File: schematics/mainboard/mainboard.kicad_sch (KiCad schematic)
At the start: 105 parts, among them J1 SD_Card_Receptacle, J2 LCD_CONN, J3 USB_C_Receptacle_USB2.0_16P, J4 BATTERY_CONN, J5 527461671, J6 SPEAKER_CONN, J9 AudioJack3, P1 1-1473005-4, U1 AMS1117-3.3, U10 PCA9555PW, U2 AMS1117-3.3, U3 MAX3421EETJ_T, U5 AMS1117-1.8, U6 TPS63002, U7 BQ24072RGT, U9 TPS22917DBV, Y1 12MHz

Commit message: Some work on mainboard pcb, most bodges resolved.
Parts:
- added C44: 0.1uF, Capacitor_SMD:C_0805_2012Metric_Pad1.18x1.45mm_HandSolder, symbol Device:C
- added C45: 47uF, Capacitor_Tantalum_SMD:CP_EIA-3216-18_Kemet-A, symbol Device:C_Polarized
- added C46, C47: 47uF, Capacitor_SMD:C_0805_2012Metric_Pad1.18x1.45mm_HandSolder, symbol Device:C
- added FB1: FerriteBead, Inductor_SMD:L_Ferrocore_DLG-0504, symbol Device:FerriteBead
- added J7: Conn_01x06, Connector_PinHeader_2.54mm:PinHeader_1x06_P2.54mm_Vertical, symbol Connector_Generic:Conn_01x06
- added R29: 0, Resistor_SMD:R_0805_2012Metric_Pad1.20x1.40mm_HandSolder, symbol Device:R
- added U12: ADS1113IDGS, Package_SO:TSSOP-10_3x3mm_P0.5mm, symbol Analog_ADC:ADS1113IDGS
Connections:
- net 3V3: now also C44.1, U12.8 (VDD)
- net 5V0: now also C45.1, FB1.2; no longer U6.1 (VOUT), U6.10 (FB)
- net BAT+: now also U12.4 (AIN0)
- net GND: now also C44.2, C45.2, J7.1 (Pin_1), U12.1 (ADDR), U12.3 (GND), U12.5 (AIN1)
- net I2C_SCL: now also U12.10 (SCL)
- net I2C_SDA: now also U12.9 (SDA)
- net USB_VBUS: now also R29.2
- net at J9.R: now also C47.2; no longer U8.30 (HPR)
- net at U8.27 (HPL): now also C47.1; no longer J9.T
- net at C5.2, U3.22 (VBCOMP): now also R29.1
- net at P1.74: now also J7.2 (Pin_2)
- net at P1.76: now also J7.3 (Pin_3)
- net at P1.78: now also J7.4 (Pin_4)
- net at P1.80: now also J7.5 (Pin_5)
- net at P1.82: now also J7.6 (Pin_6)
- net LCD_PROG_DATA: no longer names the net of J2.37 (Pin_37)
- net LCD_PROG_DATA: no longer P1.104
- net LCD_TOUCH_CLK: no longer names the net of J2.23 (Pin_23)
- net LCD_TOUCH_CLK: no longer P1.102
- net LCD_TOUCH_DATA: no longer names the net of J2.19 (Pin_19)
- net LCD_TOUCH_DATA: no longer P1.100
- net LCD_TOUCH_INTERRUPT: no longer names the net of J2.13 (Pin_13)
- net LCD_TOUCH_INTERRUPT: no longer P1.98
- new net: C46.2, J9.T
- new net: C46.1, U8.30 (HPR)
- new net: FB1.1, U6.1 (VOUT), U6.10 (FB)
- no-connect marks 103 -> 107
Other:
- note added: "I2C address 0x48"
- note added: "TODO Battery ADC Charge signal to FPGA (open drain?) What if battery/USB are connected at the same time as "ice" USB? Power switch, larger? Headphone detection, MIC/VOLDET need to be pulled down from a R to MIC Headphone caps on +/- Done Improved bulk and filter of 5V"
- company: (none) -> Anders Pistol
- title: (none) -> RetroDÄCK
- moved on the sheet: C16, C29, C5

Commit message: More work on mainboard, mostly done but need double checking.
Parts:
- removed FB1: FerriteBead, Inductor_SMD:L_Ferrocore_DLG-0504, symbol Device:FerriteBead
- removed J9: AudioJack3, Connector_Audio:Jack_3.5mm_Switronic_ST-005-G_horizontal, symbol Connector_Audio:AudioJack3
- added R31: 10k, Resistor_SMD:R_0603_1608Metric_Pad0.98x0.95mm_HandSolder, symbol Device:R
- added U11: ~, ap_phonejack:PJ-327E-5A, symbol ap_phonejack:PJ_1
- R26: value 68 -> 120
- R27: value 30 -> 68
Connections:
- net 5V0: now also U6.1 (VOUT), U6.10 (FB)
- net GND: now also U11.1 (GND)
- net at C47.2: now also U11.3 (R)
- net at C46.2: now also U11.4 (S)
- net at P1.74: now also J7.6 (Pin_6); no longer J7.2 (Pin_2)
- net at P1.76: now also J7.5 (Pin_5); no longer J7.3 (Pin_3)
- net at P1.80: now also J7.3 (Pin_3); no longer J7.5 (Pin_5)
- net at P1.82: now also J7.2 (Pin_2); no longer J7.6 (Pin_6)
- net at U8.11 (VOL/MICDET): now also R31.2, U11.5 (DETECT_GND)
- net at U8.12 (MICBIAS): now also R31.1
- no-connect marks 107 -> 106
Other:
- moved on the sheet: J7

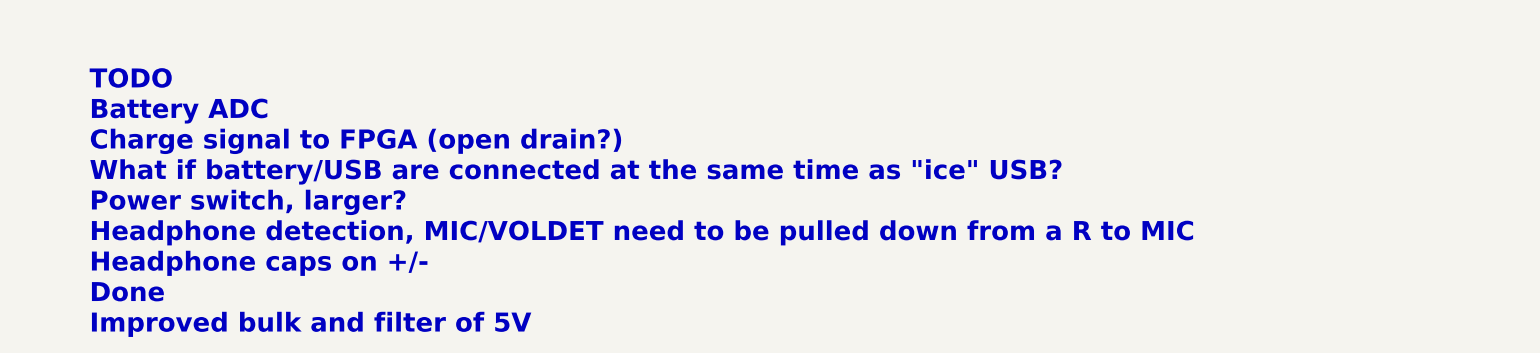
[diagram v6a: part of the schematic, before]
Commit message: Slikscreen fixes.
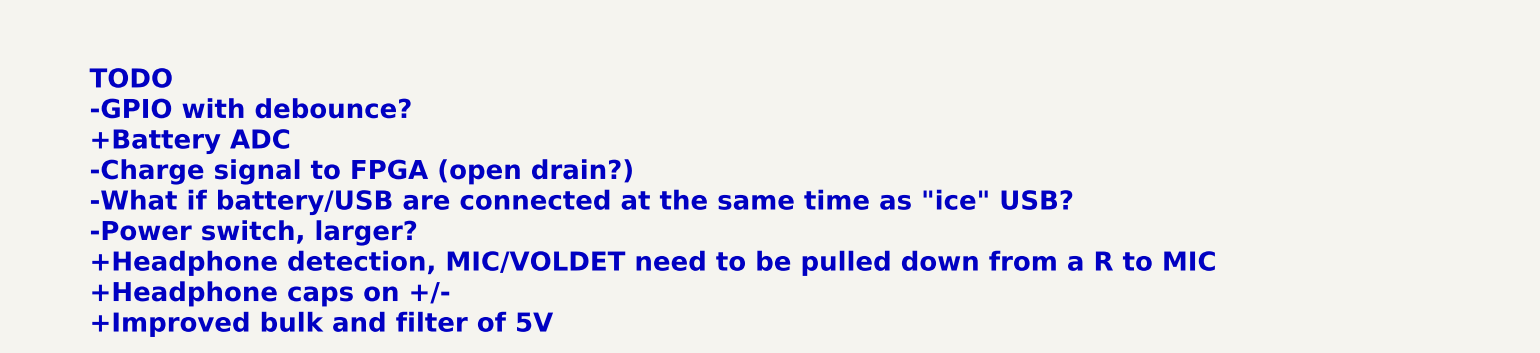
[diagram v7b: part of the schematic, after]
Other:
- note added: "TODO -GPIO with debounce? +Battery ADC -Charge signal to FPGA (open drain?) -What if battery/USB are connected at the same time as "ice" USB? -Power switch, larger? +Headphone detection, MIC/VOLDET need to be pulled down from a R to MIC +Headphone caps on +/- +Improved bulk and filter of 5V"
- note removed: "TODO Battery ADC Charge signal to FPGA (open drain?) What if battery/USB are connected at the same time as "ice" USB? Power switch, larger? Headphone detection, MIC/VOLDET need to be pulled down from a R to MIC Headphone caps on +/- Done Improved bulk and filter of 5V"
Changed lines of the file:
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@@
 		)
 	)
-	(text "TODO\nBattery ADC\nCharge signal to FPGA (open drain?)\nWhat if battery/USB are connected at the same time as \"ice\" USB?\nPower switch, larger?\nHeadphone detection, MIC/VOLDET need to be pulled down from a R to MIC\nHeadphone caps on +/- \nDone\nImproved bulk and filter of 5V"
+	(text "TODO\n-GPIO with debounce?\n+Battery ADC\n-Charge signal to FPGA (open drain?)\n-What if battery/USB are connected at the same time as \"ice\" USB?\n-Power switch, larger?\n+Headphone detection, MIC/VOLDET need to be pulled down from a R to MIC\n+Headphone caps on +/- \n+Improved bulk and filter of 5V"
 		(exclude_from_sim no)
 		(at 179.832 634.238 0)

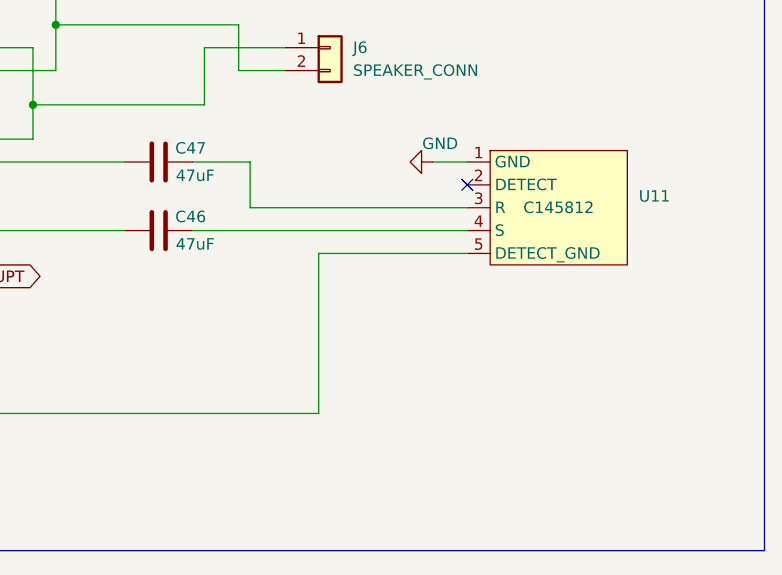
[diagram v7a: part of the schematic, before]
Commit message: Minor tweaks to mainboard, 1 mm narrower at the widest position allow for proper on/off switch. Double checked the phone jack connections.
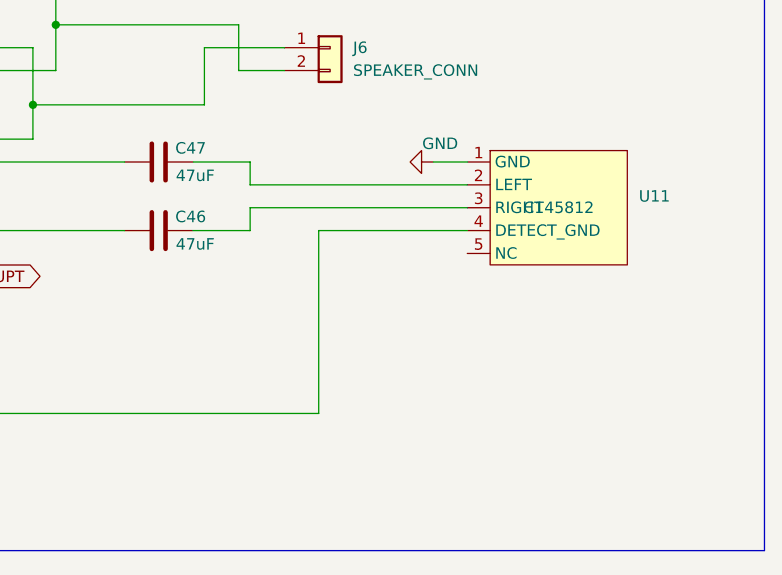
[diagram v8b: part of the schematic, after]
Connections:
- net at C47.2: now also U11.2 (LEFT); no longer U11.3 (R)
- net at C46.2: now also U11.3 (RIGHT); no longer U11.4 (S)
- net at R31.2, U8.11 (VOL/MICDET): now also U11.4 (DETECT_GND); no longer U11.5 (DETECT_GND)
- no-connect marks 106 -> 105
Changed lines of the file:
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@@
 	)
 	(no_connect
-		(at 783.59 180.34)
-	)
-	(no_connect
 		(at 365.76 262.89)
 	)
@@
 	(wire
 		(pts
+			(xy 759.46 180.34) (xy 783.59 180.34)
+		)
+		(stroke
+			(width 0)
+			(type default)
+		)
+	)
+	(wire
+		(pts
 			(xy 49.53 426.72) (xy 90.17 426.72)
 		)
@@
 	(wire
 		(pts
+			(xy 759.46 182.88) (xy 759.46 185.42)
+		)
+		(stroke
+			(width 0)
+			(type default)
+		)
+	)
+	(wire
+		(pts
 			(xy 396.24 382.27) (xy 400.05 382.27)
 		)
@@
 	(wire
 		(pts
-			(xy 767.08 187.96) (xy 783.59 187.96)
+			(xy 783.59 185.42) (xy 767.08 185.42)
 		)
 		(stroke
@@
 	(wire
 		(pts
-			(xy 753.11 185.42) (xy 783.59 185.42)
+			(xy 753.11 185.42) (xy 759.46 185.42)
 		)
 		(stroke
@@
 	(wire
 		(pts
-			(xy 759.46 182.88) (xy 783.59 182.88)
-		)
-		(stroke
-			(width 0)
-			(type default)
-		)
-	)
-	(wire
-		(pts
 			(xy 102.87 217.17) (xy 105.41 217.17)
 		)
@@
 	(wire
 		(pts
+			(xy 783.59 182.88) (xy 759.46 182.88)
+		)
+		(stroke
+			(width 0)
+			(type default)
+		)
+	)
+	(wire
+		(pts
 			(xy 361.95 382.27) (xy 365.76 382.27)
 		)
@@
 	(wire
 		(pts
-			(xy 759.46 177.8) (xy 759.46 182.88)
+			(xy 759.46 177.8) (xy 759.46 180.34)
 		)
 		(stroke
@@
 	(wire
 		(pts
-			(xy 767.08 205.74) (xy 767.08 187.96)
-		)
-		(stroke
-			(width 0)
-			(type default)
-		)
-	)
-	(wire
-		(pts
 			(xy 104.14 312.42) (xy 107.95 312.42)
 		)
@@
 	(wire
 		(pts
+			(xy 767.08 185.42) (xy 767.08 205.74)
+		)
+		(stroke
+			(width 0)
+			(type default)
+		)
+	)
+	(wire
+		(pts
 			(xy 593.09 82.55) (xy 593.09 85.09)
 		)
@@
 		)
 		(property "Footprint" "ap_phonejack:PJ-327E-5A"
-			(at 793.75 182.88 0)
+			(at 793.242 173.736 0)
 			(effects
 				(font
